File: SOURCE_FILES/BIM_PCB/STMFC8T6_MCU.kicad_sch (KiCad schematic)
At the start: 41 parts, among them J2 Conn_02x03_Odd_Even, J8 Conn_01x06, SW1 reset, U2 STM32F103C8Tx, Y1 8MHz, Y2 32.678KHz

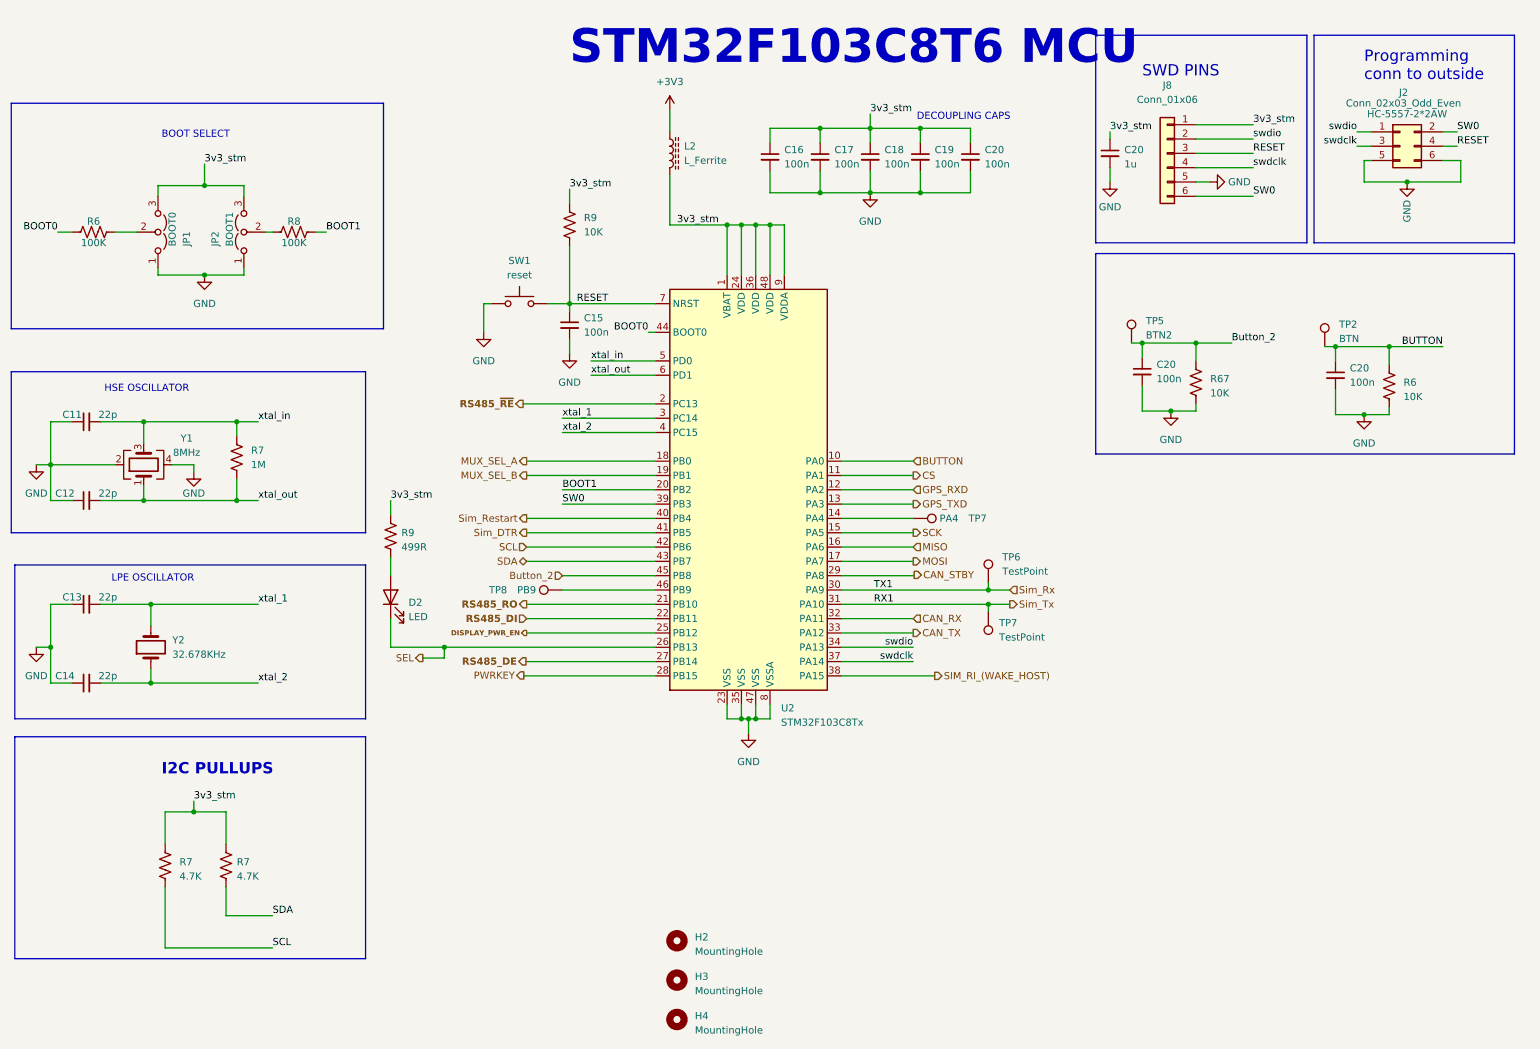
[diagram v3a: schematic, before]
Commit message: update to A9G and connector
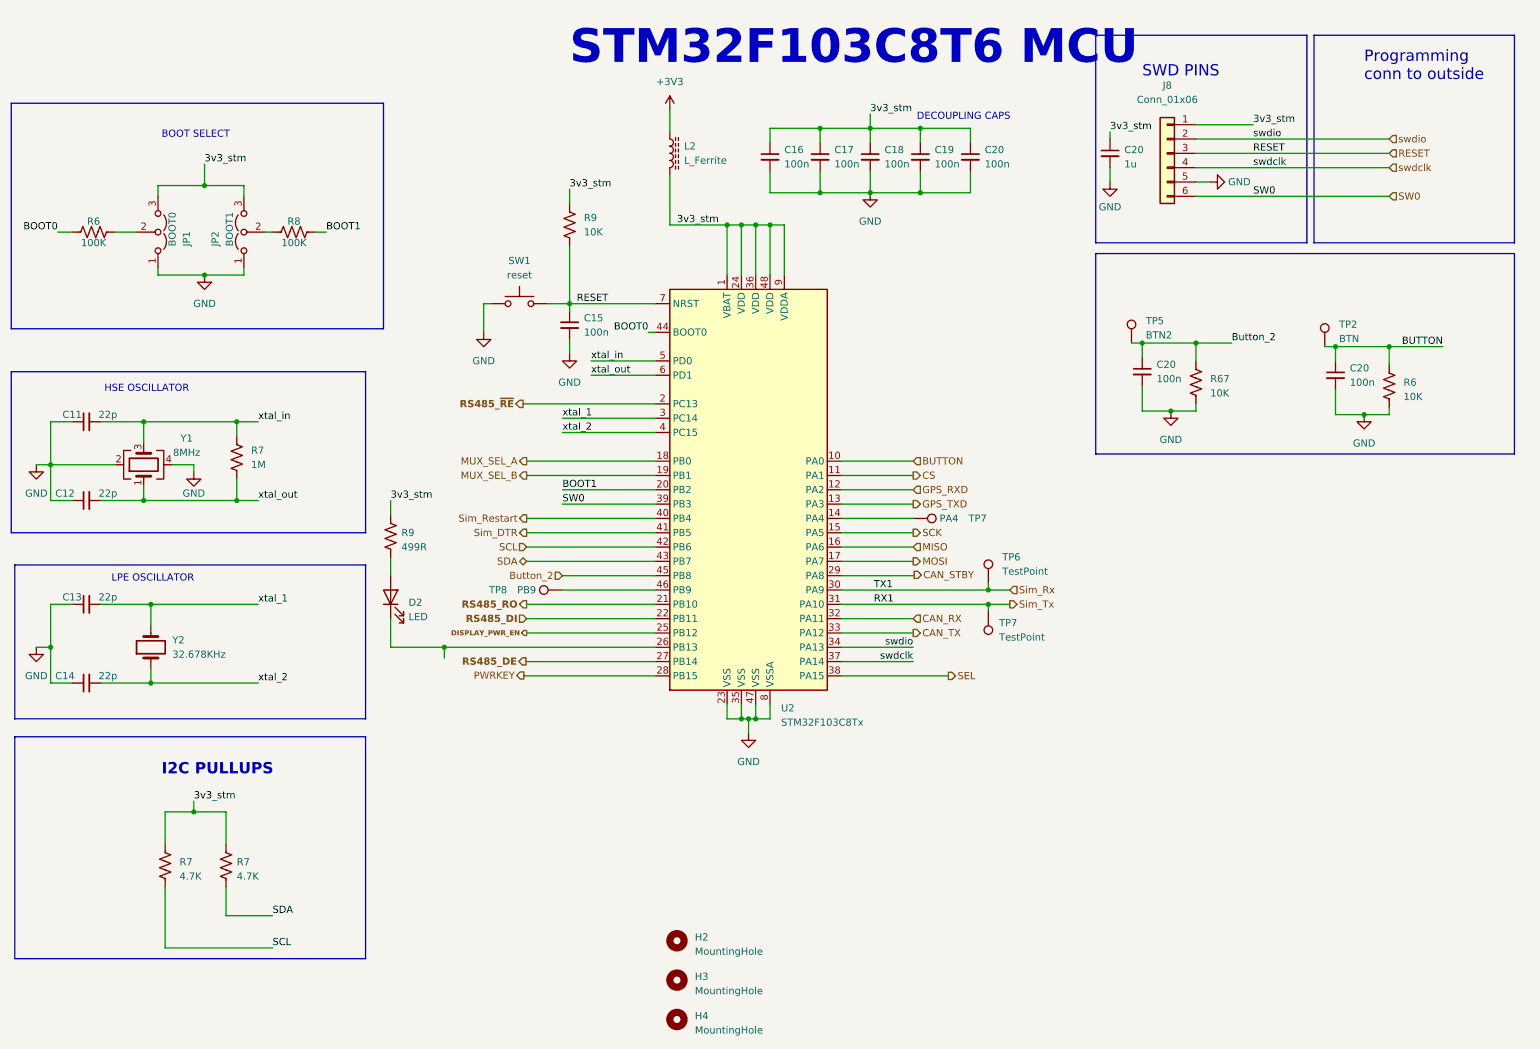
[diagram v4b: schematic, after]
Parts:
- removed J2: Conn_02x03_Odd_Even, Connector_Molex:Molex_Nano-Fit_105314-xx06_2x03_P2.50mm_Horizontal, symbol Connector_Generic:Conn_02x03_Odd_Even
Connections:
- net SIM_RI_(WAKE_HOST) is gone; now on net SEL: U2.38 (PA15)
- net SEL: no longer D2.1 (K), U2.26 (PB13)
- new net: D2.1 (K), U2.26 (PB13)
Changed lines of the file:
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@@
   (junction (at 49.53 155.575) (diameter 0) (color 0 0 0 0)
   )
-  (junction (at 264.795 43.815) (diameter 0) (color 0 0 0 0)
-  )
   (junction (at 190.5 116.205) (diameter 0) (color 0 0 0 0)
   )
@@
     (stroke (width 0) (type default))
   )
-  (wire (pts (xy 257.175 43.815) (xy 257.175 40.005))
-    (stroke (width 0) (type default))
-  )
   (wire (pts (xy 49.53 153.67) (xy 49.53 155.575))
     (stroke (width 0) (type default))
@@
     (stroke (width 0) (type default))
   )
-  (wire (pts (xy 274.32 43.815) (xy 274.32 40.005))
-    (stroke (width 0) (type default))
-  )
   (wire (pts (xy 43.18 44.45) (xy 51.435 44.45))
     (stroke (width 0) (type default))
@@
     (stroke (width 0) (type default))
   )
-  (wire (pts (xy 90.17 128.27) (xy 93.98 128.27))
-    (stroke (width 0) (type default))
-  )
   (wire (pts (xy 151.765 136.525) (xy 151.765 139.065))
     (stroke (width 0) (type default))
@@
     (stroke (width 0) (type default))
   )
-  (wire (pts (xy 274.32 40.005) (xy 271.145 40.005))
-    (stroke (width 0) (type default))
-  )
   (wire (pts (xy 93.98 126.365) (xy 131.445 126.365))
     (stroke (width 0) (type default))
@@
     (stroke (width 0) (type default))
   )
-  (wire (pts (xy 227.33 46.355) (xy 237.49 46.355))
-    (stroke (width 0) (type default))
-  )
   (wire (pts (xy 261.62 76.2) (xy 261.62 73.025))
     (stroke (width 0) (type default))
@@
     (stroke (width 0) (type default))
   )
-  (wire (pts (xy 164.465 131.445) (xy 180.975 131.445))
+  (wire (pts (xy 164.465 131.445) (xy 183.4075 131.445))
     (stroke (width 0) (type default))
   )
@@
     (stroke (width 0) (type default))
   )
-  (wire (pts (xy 273.685 34.925) (xy 271.145 34.925))
-    (stroke (width 0) (type default))
-  )
   (wire (pts (xy 45.72 93.98) (xy 49.53 93.98))
     (stroke (width 0) (type default))
@@
     (stroke (width 0) (type default))
   )
-  (wire (pts (xy 257.175 43.815) (xy 264.795 43.815))
-    (stroke (width 0) (type default))
-  )
   (wire (pts (xy 146.685 136.525) (xy 146.685 139.065))
     (stroke (width 0) (type default))
@@
     (stroke (width 0) (type default))
   )
-  (wire (pts (xy 227.33 36.195) (xy 237.49 36.195))
-    (stroke (width 0) (type default))
-  )
   (wire (pts (xy 164.465 128.905) (xy 177.165 128.905))
     (stroke (width 0) (type default))
@@
     (stroke (width 0) (type default))
   )
-  (wire (pts (xy 264.795 43.815) (xy 274.32 43.815))
-    (stroke (width 0) (type default))
-  )
   (wire (pts (xy 40.64 100.33) (xy 40.64 97.79))
     (stroke (width 0) (type default))
@@
     (stroke (width 0) (type default))
   )
-  (wire (pts (xy 255.905 34.925) (xy 258.445 34.925))
+  (wire (pts (xy 227.33 36.195) (xy 261.62 36.195))
     (stroke (width 0) (type default))
   )
@@
     (stroke (width 0) (type default))
   )
-  (wire (pts (xy 257.175 40.005) (xy 258.445 40.005))
-    (stroke (width 0) (type default))
-  )
   (wire (pts (xy 164.465 108.585) (xy 177.165 108.585))
     (stroke (width 0) (type default))
@@
     (stroke (width 0) (type default))
   )
-  (wire (pts (xy 255.905 37.465) (xy 258.445 37.465))
-    (stroke (width 0) (type default))
-  )
   (wire (pts (xy 252.095 73.025) (xy 261.62 73.025))
     (stroke (width 0) (type default))
@@
     (stroke (width 0) (type default))
   )
-  (wire (pts (xy 227.33 41.275) (xy 237.49 41.275))
+  (wire (pts (xy 227.33 41.275) (xy 261.62 41.275))
     (stroke (width 0) (type default))
   )
@@
     (stroke (width 0) (type default))
   )
-  (wire (pts (xy 273.685 37.465) (xy 271.145 37.465))
+  (wire (pts (xy 227.33 38.735) (xy 261.62 38.735))
     (stroke (width 0) (type default))
   )
@@
     (stroke (width 0) (type default))
   )
-  (wire (pts (xy 227.33 38.735) (xy 237.49 38.735))
+  (wire (pts (xy 227.33 46.355) (xy 261.62 46.355))
     (stroke (width 0) (type default))
   )
@@
     (effects (font (size 1.27 1.27)) (justify left bottom))
   )
-  (label "RESET" (at 273.685 37.465 0) (fields_autoplaced)
-    (effects (font (size 1.27 1.27)) (justify left bottom))
-  )
   (label "TX1" (at 170.18 116.205 0) (fields_autoplaced)
     (effects (font (size 1.27 1.27)) (justify left bottom))
@@
     (effects (font (size 1.27 1.27)) (justify left bottom))
   )
-  (label "swdio" (at 255.905 34.925 180) (fields_autoplaced)
-    (effects (font (size 1.27 1.27)) (justify right bottom))
-  )
   (label "xtal_in" (at 120.015 75.565 0) (fields_autoplaced)
-    (effects (font (size 1.27 1.27)) (justify left bottom))
-  )
-  (label "SW0" (at 273.685 34.925 0) (fields_autoplaced)
     (effects (font (size 1.27 1.27)) (justify left bottom))
   )
@@
     (effects (font (size 1.27 1.27)) (justify left bottom))
   )
-  (label "swdclk" (at 255.905 37.465 180) (fields_autoplaced)
-    (effects (font (size 1.27 1.27)) (justify right bottom))
-  )
   (label "xtal_out" (at 120.015 78.105 0) (fields_autoplaced)
     (effects (font (size 1.27 1.27)) (justify left bottom))
@@
     (effects (font (size 1.27 1.27)) (justify left bottom))
   )
-  (hierarchical_label "SEL" (shape output) (at 90.17 128.27 180) (fields_autoplaced)
-    (effects (font (size 1.27 1.27)) (justify right))
+  (hierarchical_label "SEL" (shape output) (at 183.4075 131.445 0) (fields_autoplaced)
+    (effects (font (size 1.27 1.27)) (justify left))
   )
   (hierarchical_label "CAN_STBY" (shape output) (at 177.336 113.5232 0) (fields_autoplaced)
@@
     (effects (font (size 1.27 1.27)) (justify left))
   )
+  (hierarchical_label "SW0" (shape input) (at 261.62 46.355 0) (fields_autoplaced)
+    (effects (font (size 1.27 1.27)) (justify left))
+  )
   (hierarchical_label "Sim_Restart" (shape output) (at 108.585 103.505 180) (fields_autoplaced)
     (effects (font (size 1.27 1.27)) (justify right))
   )
+  (hierarchical_label "swdclk" (shape input) (at 261.62 41.275 0) (fields_autoplaced)
+    (effects (font (size 1.27 1.27)) (justify left))
+  )
+  (hierarchical_label "swdio" (shape input) (at 261.62 36.195 0) (fields_autoplaced)
+    (effects (font (size 1.27 1.27)) (justify left))
+  )
   (hierarchical_label "Sim_Rx" (shape input) (at 194.31 116.205 0) (fields_autoplaced)
     (effects (font (size 1.27 1.27)) (justify left))
@@
     (effects (font (size 1.27 1.27)) (justify right))
   )
+  (hierarchical_label "RESET" (shape input) (at 261.62 38.735 0) (fields_autoplaced)
+    (effects (font (size 1.27 1.27)) (justify left))
+  )
   (hierarchical_label "RS485_DE" (shape output) (at 108.4632 128.8757 180) (fields_autoplaced)
     (effects (font (size 1.27 1.27) bold) (justify right))
@@
     (effects (font (size 1.27 1.27) bold) (justify right))
   )
-  (hierarchical_label "SIM_RI_(WAKE_HOST)" (shape output) (at 180.975 131.445 0) (fields_autoplaced)
-    (effects (font (size 1.27 1.27)) (justify left))
-  )
   (hierarchical_label "SCL" (shape input) (at 108.585 108.585 180) (fields_autoplaced)
     (effects (font (size 1.27 1.27)) (justify right))
@@
         (path "/b79ebed7-e146-448b-8dab-0aefb3e182ca/f23c600c-7725-4edd-91d3-0267a41a1c43"
           (reference "#PWR018") (unit 1)
-        )
-      )
-    )
-  )
-  (symbol (lib_id "Connector_Generic:Conn_02x03_Odd_Even") (at 263.525 37.465 0) (unit 1)
-    (in_bom yes) (on_board yes) (dnp no)
-    (property "Reference" "J2" (at 264.16 27.94 0)
-      (effects (font (size 1.27 1.27)))
-    )
-    (property "Value" "Conn_02x03_Odd_Even" (at 264.16 29.845 0)
-      (effects (font (size 1.27 1.27)))
-    )
-    (property "Footprint" "Connector_Molex:Molex_Nano-Fit_105314-xx06_2x03_P2.50mm_Horizontal" (at 263.525 37.465 0)
-      (effects (font (size 1.27 1.27)) hide)
-    )
-    (property "Datasheet" "~" (at 263.525 37.465 0)
-      (effects (font (size 1.27 1.27)) hide)
-    )
-    (property "MPN" "HC-5557-2*2AW" (at 264.795 31.75 0)
-      (effects (font (size 1.27 1.27)))
-    )
-    (pin "1")
-    (pin "2")
-    (pin "3")
-    (pin "4")
-    (pin "5")
-    (pin "6")
-    (instances
-      (project "BIM_PCB"
-        (path "/b79ebed7-e146-448b-8dab-0aefb3e182ca/f23c600c-7725-4edd-91d3-0267a41a1c43"
-          (reference "J2") (unit 1)
         )
       )
@@
         )
       )
-    )
-  )
-  (symbol (lib_id "power:GND") (at 264.795 43.815 0) (unit 1)
-    (in_bom yes) (on_board yes) (dnp no)
-    (property "Reference" "#PWR025" (at 264.795 50.165 0)
-      (effects (font (size 1.27 1.27)) hide)
-    )
-    (property "Value" "GND" (at 264.795 46.99 90)
-      (effects (font (size 1.27 1.27)) (justify right))
-    )
-    (property "Footprint" "" (at 264.795 43.815 0)
-      (effects (font (size 1.27 1.27)) hide)
-    )
-    (property "Datasheet" "" (at 264.795 43.815 0)
-      (effects (font (size 1.27 1.27)) hide)
-    )
-    (pin "1")
-    (instances
-      (project "ALERT_RIDER_HARDWARE"
-        (path "/6bd12930-91c7-432a-9f98-f9ae5061d3a7/d867153f-866e-4815-8450-e9b125a4b7ea"
-          (reference "#PWR025") (unit 1)
-        )
-      )
-      (project "BIM_PCB"
-        (path "/b79ebed7-e146-448b-8dab-0aefb3e182ca/f23c600c-7725-4edd-91d3-0267a41a1c43"
-          (reference "#PWR07") (unit 1)
-        )
-      )

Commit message: all items updated
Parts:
- D2: footprint LED_SMD:LED_0603_1608Metric -> LED_SMD:LED_0402_1005Metric
- L2: footprint Inductor_SMD:L_0603_1608Metric -> Inductor_SMD:L_0402_1005Metric
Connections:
- net CAN_RX: now also U2.22 (PB11); no longer U2.32 (PA11)
- net CAN_TX: now also U2.21 (PB10); no longer U2.33 (PA12)
- net RS485_DI: now also U2.32 (PA11); no longer U2.22 (PB11)
- net RS485_RO: now also U2.33 (PA12); no longer U2.21 (PB10)
- net GPS_RXD renamed TXD
- net GPS_TXD renamed RXD
- net Sim_Rx renamed TX1
- net Sim_Tx renamed RX1
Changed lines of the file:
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@@
   (junction (at 151.765 51.435) (diameter 0) (color 0 0 0 0)
   )
-  (junction (at 93.98 126.365) (diameter 0) (color 0 0 0 0)
-  )
   (junction (at 261.62 73.025) (diameter 0) (color 0 0 0 0)
   )
@@
     (stroke (width 0) (type default))
   )
-  (wire (pts (xy 93.98 126.365) (xy 84.455 126.365))
+  (wire (pts (xy 84.455 126.365) (xy 131.445 126.365))
     (stroke (width 0) (type default))
   )
@@
     (stroke (width 0) (type default))
   )
-  (wire (pts (xy 93.98 126.365) (xy 131.445 126.365))
-    (stroke (width 0) (type default))
-  )
   (wire (pts (xy 44.45 179.705) (xy 44.45 168.91))
     (stroke (width 0) (type default))
@@
   )
   (polyline (pts (xy 17.145 29.845) (xy 83.185 29.845))
-    (stroke (width 0) (type default))
-  )
-  (wire (pts (xy 93.98 128.27) (xy 93.98 126.365))
     (stroke (width 0) (type default))
   )
@@
     (effects (font (size 1.27 1.27)) (justify left))
   )
-  (hierarchical_label "GPS_TXD" (shape output) (at 177.165 100.965 0) (fields_autoplaced)
+  (hierarchical_label "TXD" (shape output) (at 177.165 98.425 0) (fields_autoplaced)
     (effects (font (size 1.27 1.27)) (justify left))
   )
@@
     (effects (font (size 1.27 1.27)) (justify left))
   )
-  (hierarchical_label "CAN_TX" (shape output) (at 177.165 123.825 0) (fields_autoplaced)
-    (effects (font (size 1.27 1.27)) (justify left))
+  (hierarchical_label "CAN_TX" (shape output) (at 108.585 118.745 180) (fields_autoplaced)
+    (effects (font (size 1.27 1.27)) (justify right))
   )
   (hierarchical_label "SW0" (shape input) (at 261.62 46.355 0) (fields_autoplaced)
@@
     (effects (font (size 1.27 1.27)) (justify left))
   )
-  (hierarchical_label "Sim_Rx" (shape input) (at 194.31 116.205 0) (fields_autoplaced)
+  (hierarchical_label "TX1" (shape output) (at 194.31 116.205 0) (fields_autoplaced)
     (effects (font (size 1.27 1.27)) (justify left))
   )
-  (hierarchical_label "RS485_RO" (shape output) (at 108.585 118.745 180) (fields_autoplaced)
-    (effects (font (size 1.27 1.27) bold) (justify right))
+  (hierarchical_label "RS485_RO" (shape output) (at 177.165 123.825 0) (fields_autoplaced)
+    (effects (font (size 1.27 1.27) bold) (justify left))
   )
   (hierarchical_label "MUX_SEL_A" (shape output) (at 108.585 93.345 180) (fields_autoplaced)
@@
     (effects (font (size 1.27 1.27)) (justify left))
   )
-  (hierarchical_label "CAN_RX" (shape input) (at 177.165 121.285 0) (fields_autoplaced)
-    (effects (font (size 1.27 1.27)) (justify left))
+  (hierarchical_label "CAN_RX" (shape input) (at 108.585 121.285 180) (fields_autoplaced)
+    (effects (font (size 1.27 1.27)) (justify right))
   )
   (hierarchical_label "PWRKEY" (shape output) (at 108.0919 131.3658 180) (fields_autoplaced)
@@
     (effects (font (size 1.27 1.27)) (justify right))
   )
-  (hierarchical_label "GPS_RXD" (shape input) (at 177.165 98.425 0) (fields_autoplaced)
+  (hierarchical_label "RXD" (shape input) (at 177.165 100.965 0) (fields_autoplaced)
     (effects (font (size 1.27 1.27)) (justify left))
   )
@@
     (effects (font (size 1.27 1.27)) (justify left))
   )
-  (hierarchical_label "RS485_DI" (shape input) (at 108.585 121.285 180) (fields_autoplaced)
-    (effects (font (size 1.27 1.27) bold) (justify right))
+  (hierarchical_label "RS485_DI" (shape input) (at 177.165 121.285 0) (fields_autoplaced)
+    (effects (font (size 1.27 1.27) bold) (justify left))
   )
   (hierarchical_label "SCL" (shape input) (at 108.585 108.585 180) (fields_autoplaced)
@@
     (effects (font (size 1.27 1.27)) (justify right))
   )
-  (hierarchical_label "Sim_Tx" (shape output) (at 194.31 118.745 0) (fields_autoplaced)
+  (hierarchical_label "RX1" (shape input) (at 194.31 118.745 0) (fields_autoplaced)
     (effects (font (size 1.27 1.27)) (justify left))
   )
@@
       (effects (font (size 1.27 1.27)) (justify right))
     )
-    (property "Footprint" "LED_SMD:LED_0603_1608Metric" (at 84.455 117.475 0)
+    (property "Footprint" "LED_SMD:LED_0402_1005Metric" (at 84.455 117.475 0)
       (effects (font (size 1.27 1.27)) hide)
     )
@@
       (effects (font (size 1.27 1.27)) (justify left))
     )
-    (property "Footprint" "Inductor_SMD:L_0603_1608Metric" (at 133.985 38.735 0)
-      (effects (font (size 1.27 1.27)) hide)
-    )
+    (property "Footprint" "Inductor_SMD:L_0402_1005Metric" (at 133.985 38.735 0)
+      (effects (font (size 1.27 1.27)) hide)
+    )
